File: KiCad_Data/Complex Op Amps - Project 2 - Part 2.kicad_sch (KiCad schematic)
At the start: 95 parts, among them P1 Potentiometer P/N: 3590P-2-**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, P2 Potentiometer P/N: 3590P-2-**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, SW1 SPST Switch, P/N: GT12MABE, SW2 SPST Switch, P/N: GT12MABE, SW3 SPST Switch, P/N: GT12MABE, SW4 SPST Switch, P/N: GT12MABE, SW5 SPST Switch, P/N: GT12MABE, T1 Transistor P/N: 2N3906, T2 Transistor P/N: 2N3906, T3 Transistor P/N: 2N3906, T4 Transistor P/N: 2N3906

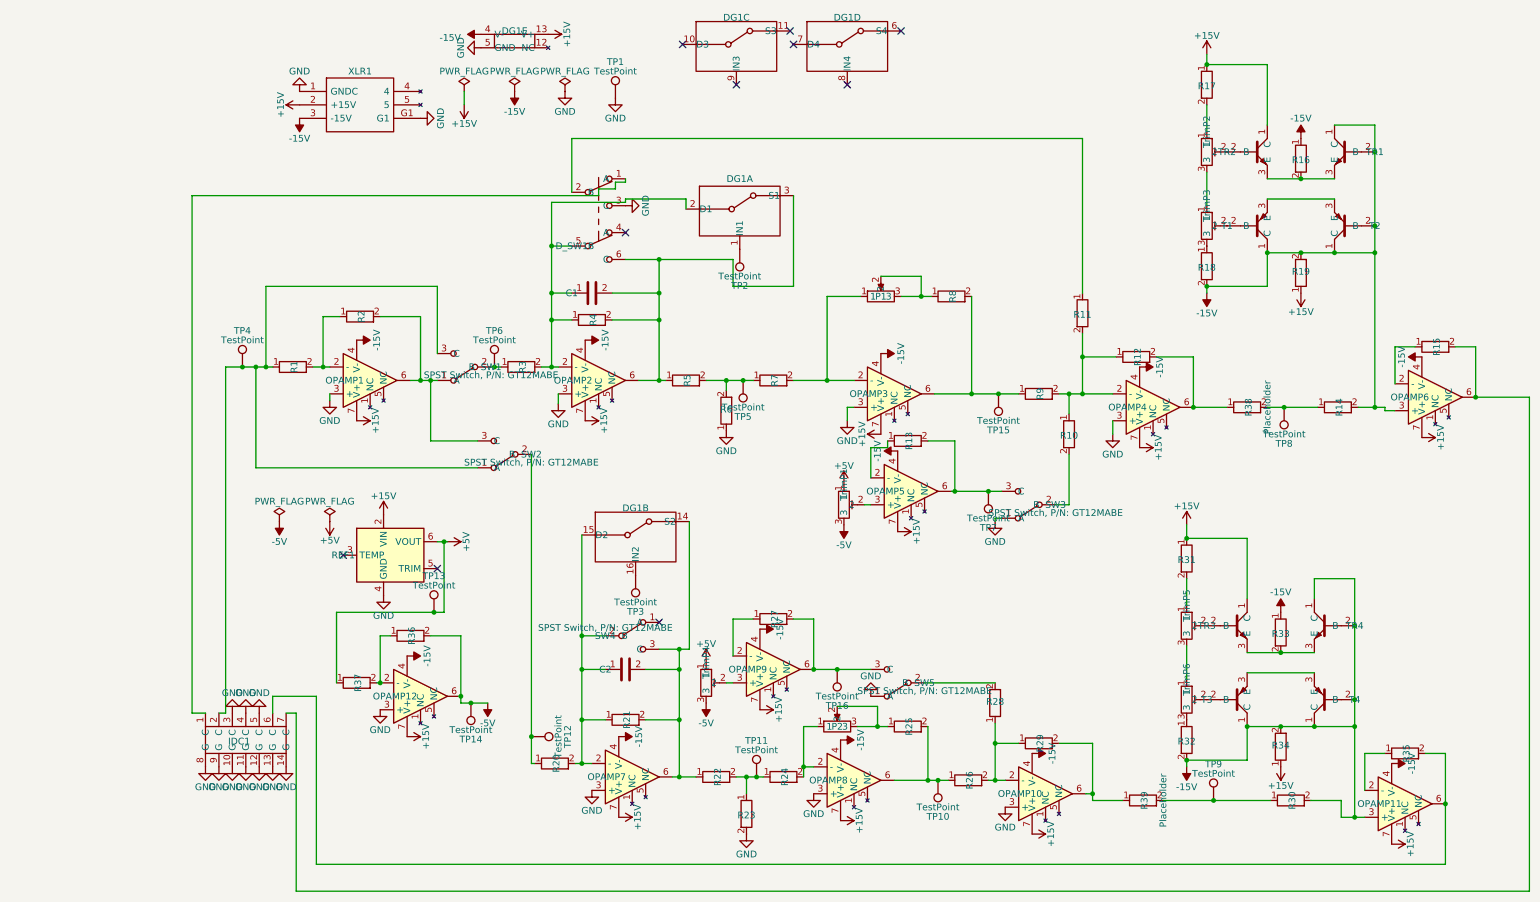
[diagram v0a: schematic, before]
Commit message: Updated files
Contain Kicad files which include the required capacitors on each op-amp, and additionally electrolytic capacitors were added
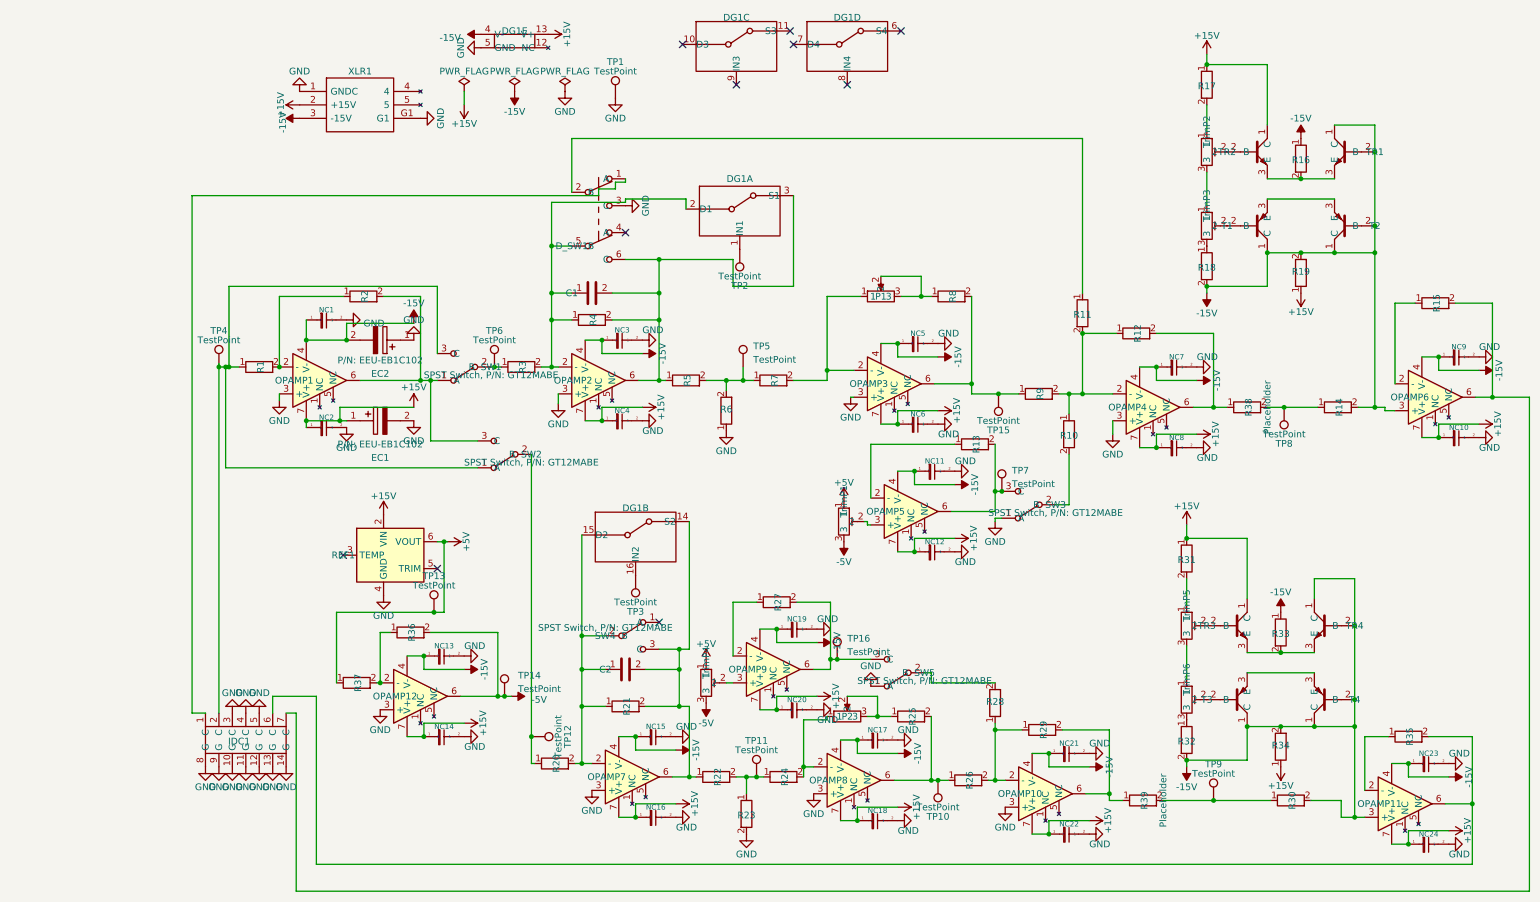
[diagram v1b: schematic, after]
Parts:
- added EC1, EC2: P/N: EEU-EB1C102, Complex_Op_Amps_Footprints:ELECTROLYTIC CAPACITOR - EEU-EB1C102, symbol Complex_Op_Amps_Footprints:EEU-EB1C102
- added NC1, NC10, NC11, NC12, NC13, NC14, NC15, NC16, NC17, NC18, NC19, NC2, NC20, NC21, NC22, NC23, NC24, NC3, NC4, NC5, NC6, NC7, NC8, NC9: Normal_Capacitor, P/N: 399-4209-ND, Complex_Op_Amps_Footprints:CAPACITOR - 399-4209-ND, symbol Complex_Op_Amps_Footprints:Normal_Capacitor_399-4209-ND
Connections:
- net +15V: now also EC1.1, NC10.1 (2), NC12.1 (2), NC14.1 (2), NC16.1 (2), NC18.1 (2), NC2.1 (2), NC20.1 (2), NC22.1 (2), NC24.1 (2), NC4.1 (2), NC6.1 (2), NC8.1 (2)
- net -15V: now also EC2.2, NC1.1 (2), NC11.1 (2), NC13.1 (2), NC15.1 (2), NC17.1 (2), NC19.1 (2), NC21.1 (2), NC23.1 (2), NC3.1 (2), NC5.1 (2), NC7.1 (2), NC9.1 (2)
- net GND: now also EC1.2, EC2.1, NC1.2 (1), NC10.2 (1), NC11.2 (1), NC12.2 (1), NC13.2 (1), NC14.2 (1), NC15.2 (1), NC16.2 (1), NC17.2 (1), NC18.2 (1), NC19.2 (1), NC2.2 (1), NC20.2 (1), NC21.2 (1), NC22.2 (1), NC23.2 (1), NC24.2 (1), NC3.2 (1), NC4.2 (1), NC5.2 (1), NC6.2 (1), NC7.2 (1), NC8.2 (1), NC9.2 (1)
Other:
- moved on the sheet: OPAMP1, OPAMP3, OPAMP5, P2, R1, R12, R13, R15, R2, R21, R25, R27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

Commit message: Updated PCB and Schematic
The PCB has the same changes as the schematic, the schematic had the DPDT switch made into 2 separate switches and capacitors were added onto the DG201 switch's
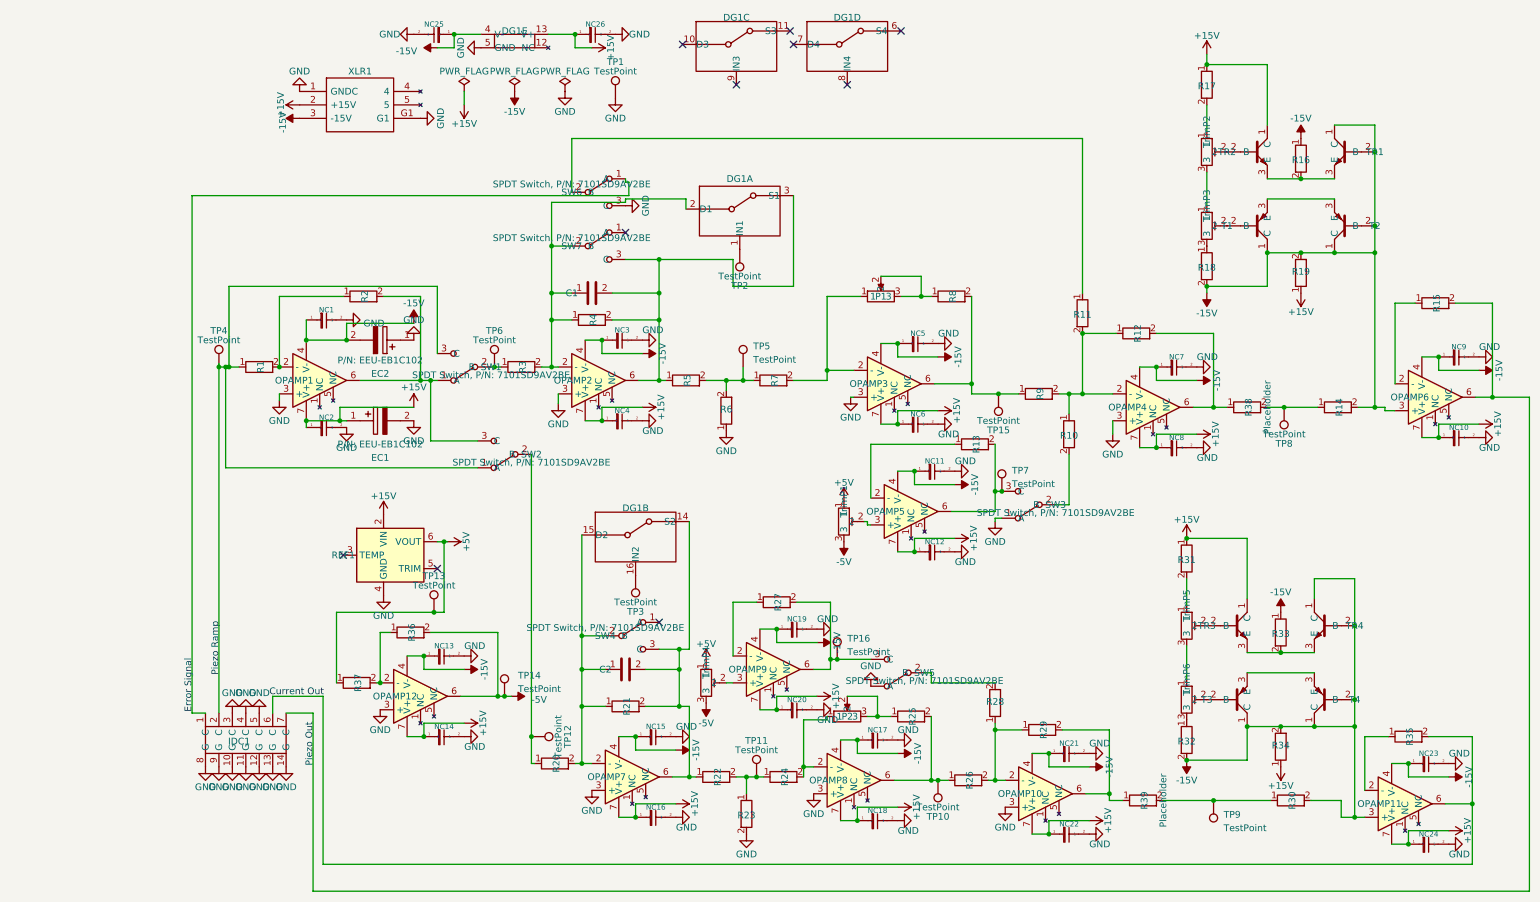
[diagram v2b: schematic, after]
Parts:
- removed D_SW1: P/N: 7101SD9AV2BE, Complex_Op_Amps_Footprints:DPDT Switch, symbol Complex_Op_Amps_Footprints:Double_Switch
- added NC25, NC26: Normal_Capacitor, P/N: 399-4209-ND, Complex_Op_Amps_Footprints:CAPACITOR - 399-4209-ND, symbol Complex_Op_Amps_Footprints:Normal_Capacitor_399-4209-ND
- added SW6, SW7: SPDT Switch, P/N: 7101SD9AV2BE, Complex_Op_Amps_Footprints:AV2_Switch, symbol Complex_Op_Amps_Footprints:Switch
- SW1, SW2, SW3, SW4, SW5: value SPST Switch, P/N: GT12MABE -> SPDT Switch, P/N: 7101SD9AV2BE
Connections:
- net +15V: now also NC26.1 (2)
- net -15V: now also NC25.1 (2)
- net GND: now also NC25.2 (1), NC26.2 (1), SW6.3 (C)
- net at C1.1, DG1.2 (D1), OPAMP2.2 (-)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: now also SW7.2 (B)
- net at C1.2, DG1.3 (S1), OPAMP2.6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: now also SW7.3 (C)
- net at IDC1.1 (C): now also SW6.1 (A)
- net at R11.1: now also SW6.2 (B)
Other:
- note added: "Current Out"
- note added: "Error Signal"
- note added: "Piezo Out"
- note added: "Piezo Ramp"
- moved on the sheet: TP9

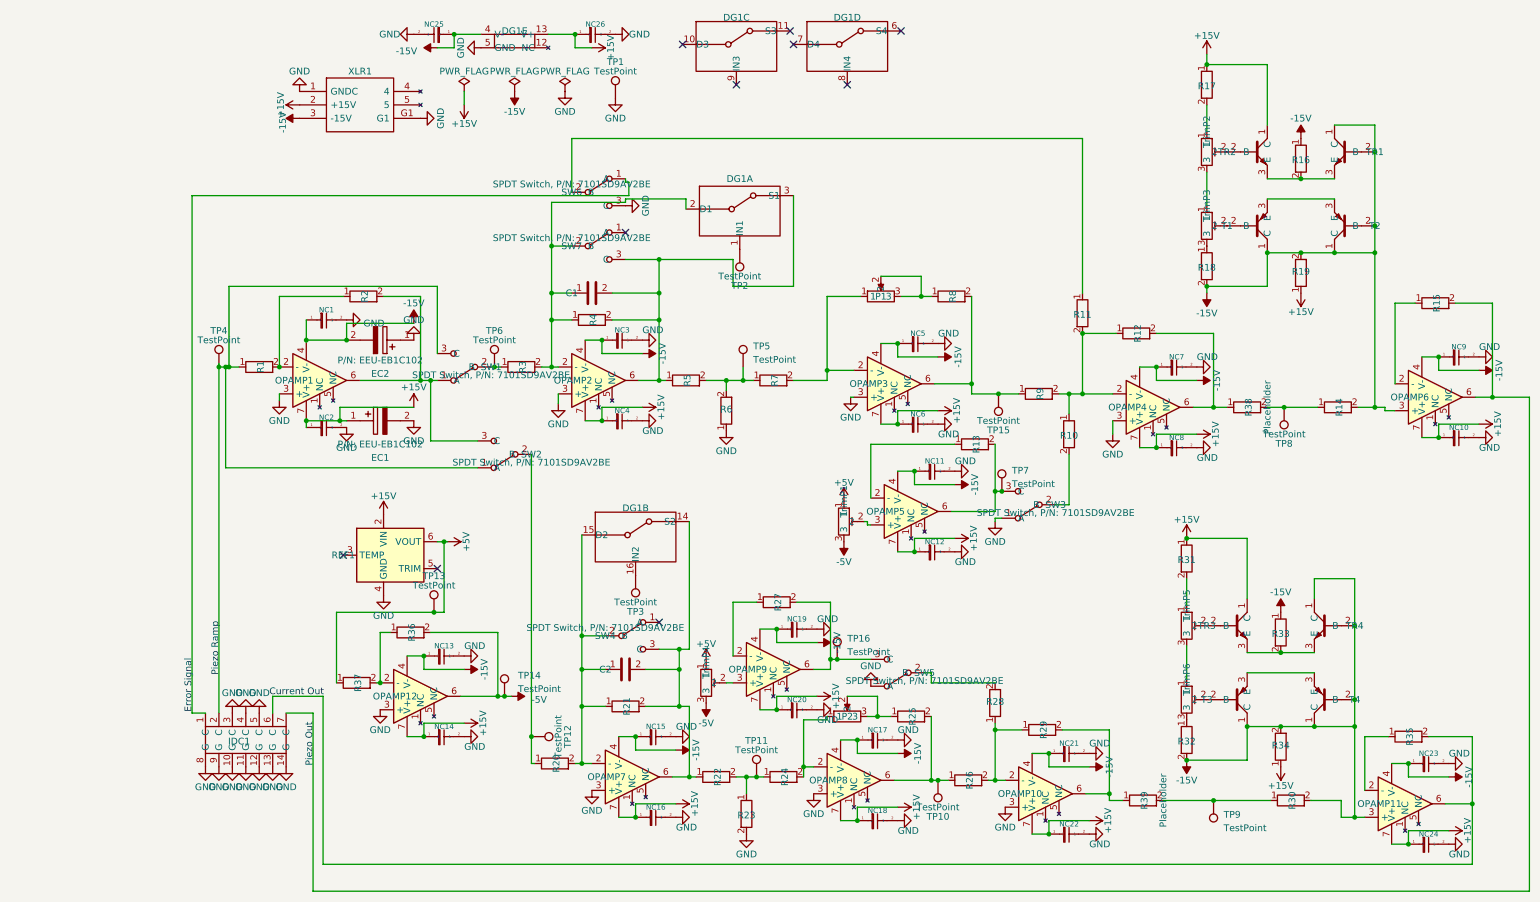
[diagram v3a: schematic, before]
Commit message: Changed Names
Naming was updated for the symbols to make more sense (adding values for resistance, what each switch does, etc)
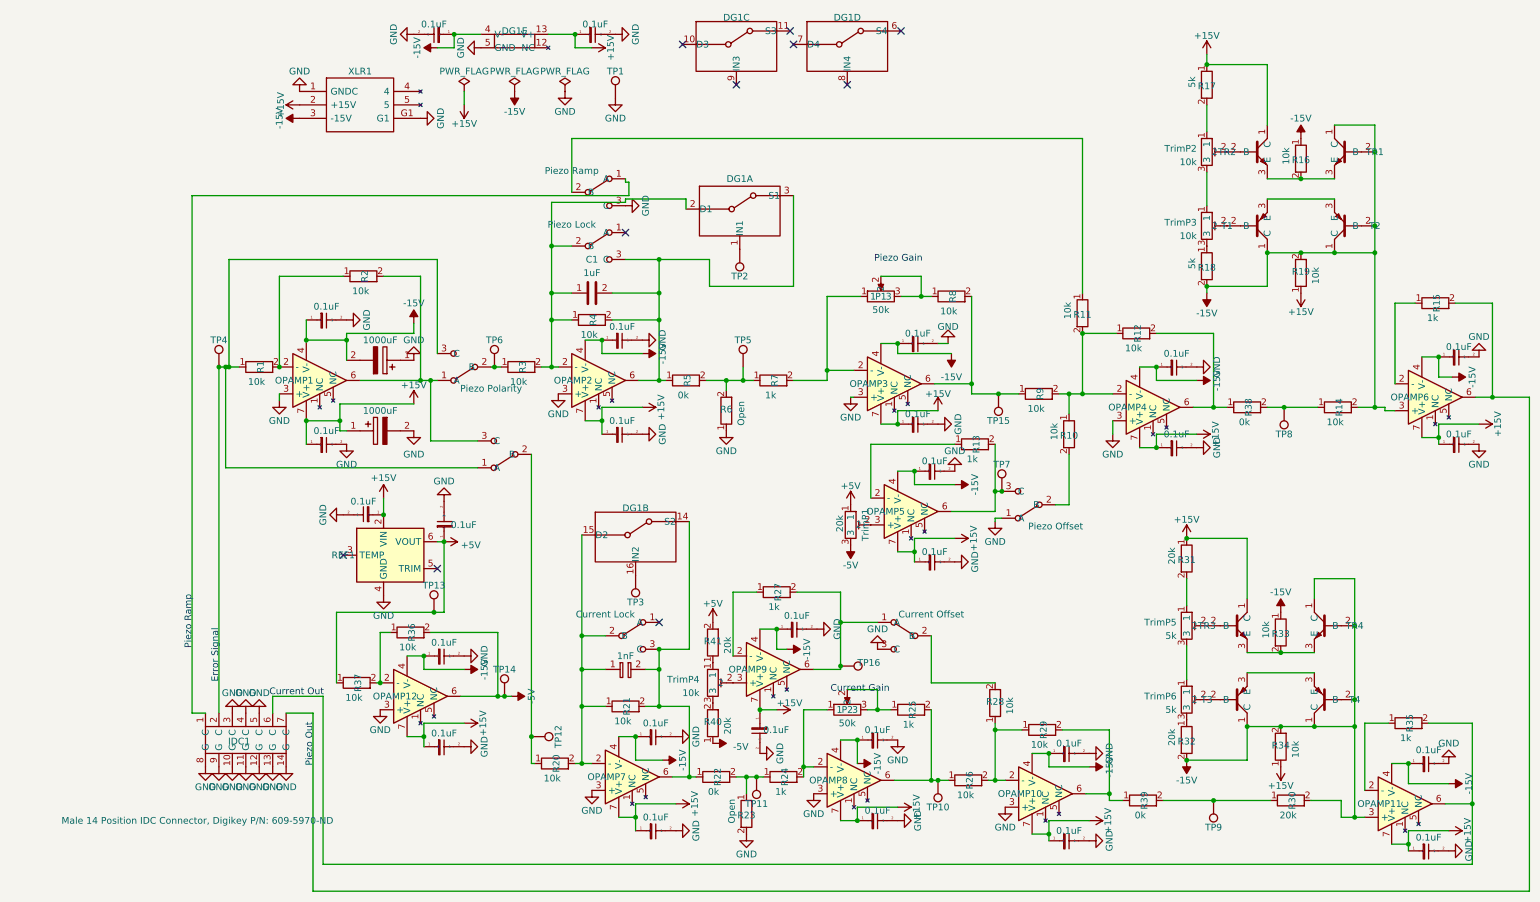
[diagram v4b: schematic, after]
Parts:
- removed C1, C2: ~, Complex_Op_Amps_Footprints:Polypropylene Capacitor, symbol Complex_Op_Amps_Footprints:Capacitor
- added C1: 1uF, Complex_Op_Amps_Footprints:Polypropylene Capacitor, symbol Complex_Op_Amps_Footprints:Ploypropylene Capacitor
- added NC27, NC28: 0.1uF, Complex_Op_Amps_Footprints:CAPACITOR - 399-4209-ND, symbol Complex_Op_Amps_Footprints:Normal_Capacitor_399-4209-ND
- added R40, R41: 20k, Complex_Op_Amps_Footprints:R_Axial_DIN0207_L6.3mm_D2.5mm_P10.16mm_Horizontal, symbol Complex_Op_Amps_Footprints:Resistor
- added SC1: 1nF, Complex_Op_Amps_Footprints:Small Capacitor, symbol Complex_Op_Amps_Footprints:Small_Capacitor
- EC1, EC2: value P/N: EEU-EB1C102 -> 1000uF
- NC1, NC10, NC11, NC12, NC13, NC14, NC15, NC16, NC17, NC18, NC19, NC2, NC20, NC21, NC22, NC23, NC24, NC25, NC26, NC3, NC4, NC5, NC6, NC7, NC8, NC9: value Normal_Capacitor, P/N: 399-4209-ND -> 0.1uF
- P1, P2: value Potentiometer P/N: 3590P-2-***L -> 50k
- R1, R10, R11, R12, R14, R16, R19, R2, R20, R21, R26, R28, R29, R3, R33, R34, R36, R37, R4, R8, R9: value Generic Resistor -> 10k
- R13, R15, R24, R25, R27, R35, R7: value Generic Resistor -> 1k
- R17, R18: value Generic Resistor -> 5k
- R22, R5: value Generic Resistor -> 0k
- R23, R6: value Generic Resistor -> Open
- R30, R31, R32: value Generic Resistor -> 20k
- R38, R39: value Generic Resistor -> 0k; Reason Placeholder -> (none)
- SW1: Name (none) -> Piezo Polarity
- SW3: Name (none) -> Piezo Offset
- SW4: Name (none) -> Current Lock
- SW5: Name (none) -> Current Offset
- SW6: Name (none) -> Piezo Ramp
- SW7: Name (none) -> Piezo Lock
- TrimP1: value P/N: 3296X-1-**** -> 20k
- TrimP2, TrimP3, TrimP4: value P/N: 3296X-1-**** -> 10k
- TrimP5, TrimP6: value P/N: 3296X-1-**** -> 5k
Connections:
- net +15V: now also NC28.1 (2)
- net +5V: now also NC27.1 (2), R41.2; no longer TrimP4.1
- net -5V: now also R40.1; no longer TrimP4.3
- net GND: now also SW5.3 (C), NC27.2 (1), NC28.2 (1); no longer SW5.1 (A)
- net at DG1.2 (D1), OPAMP2.2 (-), R3.2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: now also C1.1
- net at DG1.3 (S1), OPAMP2.6, R4.2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: now also C1.2
- net at DG1.15 (D2), OPAMP7.2 (-), R20.2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: now also SC1.1
- net at DG1.14 (S2), OPAMP7.6, R21.2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: now also SC1.2
- net at OPAMP9.6, R27.2, TP16.1: now also SW5.1 (A); no longer SW5.3 (C)
- new net: R40.2, TrimP4.3
- new net: R41.1, TrimP4.1
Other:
- note added: "Current Gain"
- note added: "Piezo Gain"
- moved on the sheet: P2, R2, R25, R27, R35, TP11, TP16, TrimP1, TrimP4

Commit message: Fixed Wiring that was close to edge
This version is our first ordered version
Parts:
- SW2: Name (none) -> Current Polarity
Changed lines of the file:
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@@
       (effects (font (size 1.27 1.27)) hide)
     )
-    (property "Name" "" (at 83.82 100.584 0)
+    (property "Name" "Current Polarity" (at 83.82 100.584 0)
       (effects (font (size 1.27 1.27)))
     )
